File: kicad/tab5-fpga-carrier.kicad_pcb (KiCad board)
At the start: 4 copper layers, 81 x 78 mm, 77 parts, among them J1 DC 12-24V, J2 USB-C PD in, J3 M5-BUS (to Tab5), J4 Tang Primer 20K Core, J5 HDMI OUT, J6 PMOD1, J7 PMOD2, J8 FPGA JTAG, Q1 2N7002, Q2 2N7002, SW1 SW, SW2 SW, U1 CH224K, U2 TPS5430DDAR, U3 AMS1117-3.3

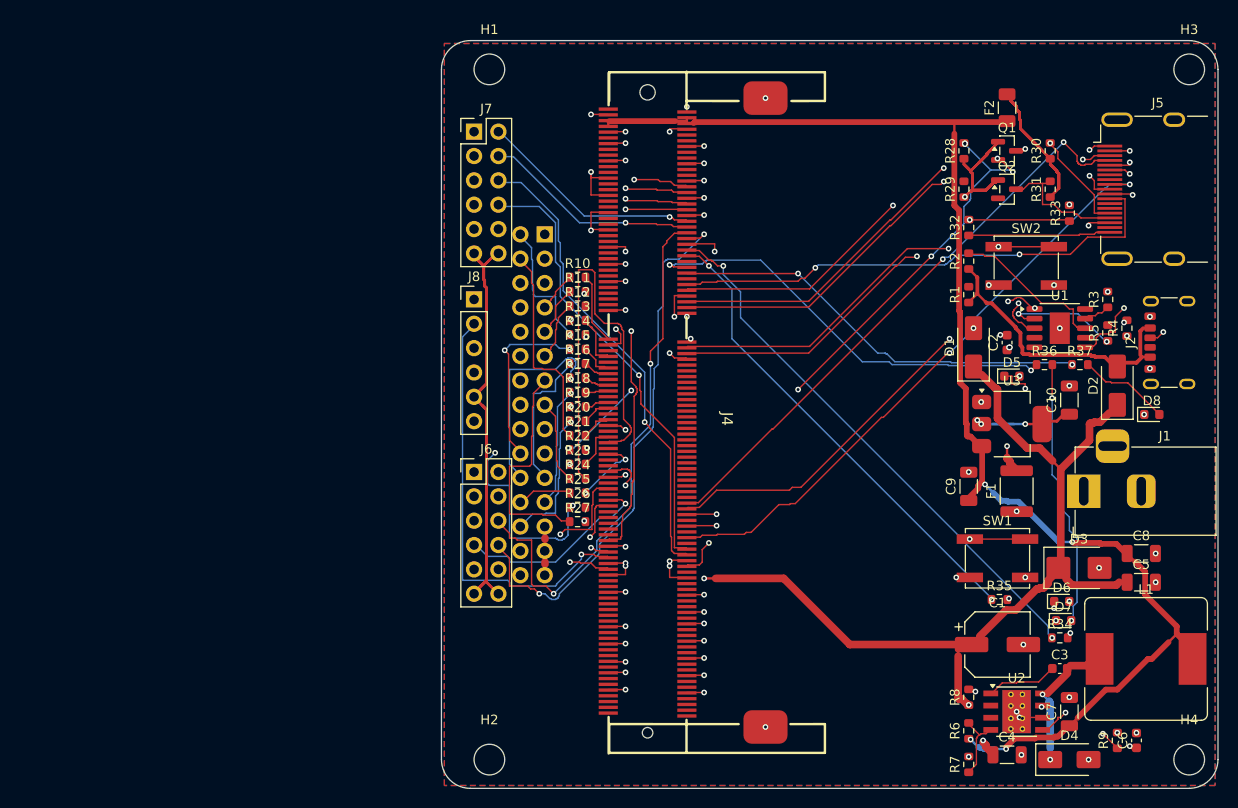
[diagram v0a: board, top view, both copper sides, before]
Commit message: kicad: 103/103 nets routed (rip-up router), DRC clean; BOM; finish script; site update
Co-Authored-By: Claude Sonnet 5.5 <noreply@anthropic.com>
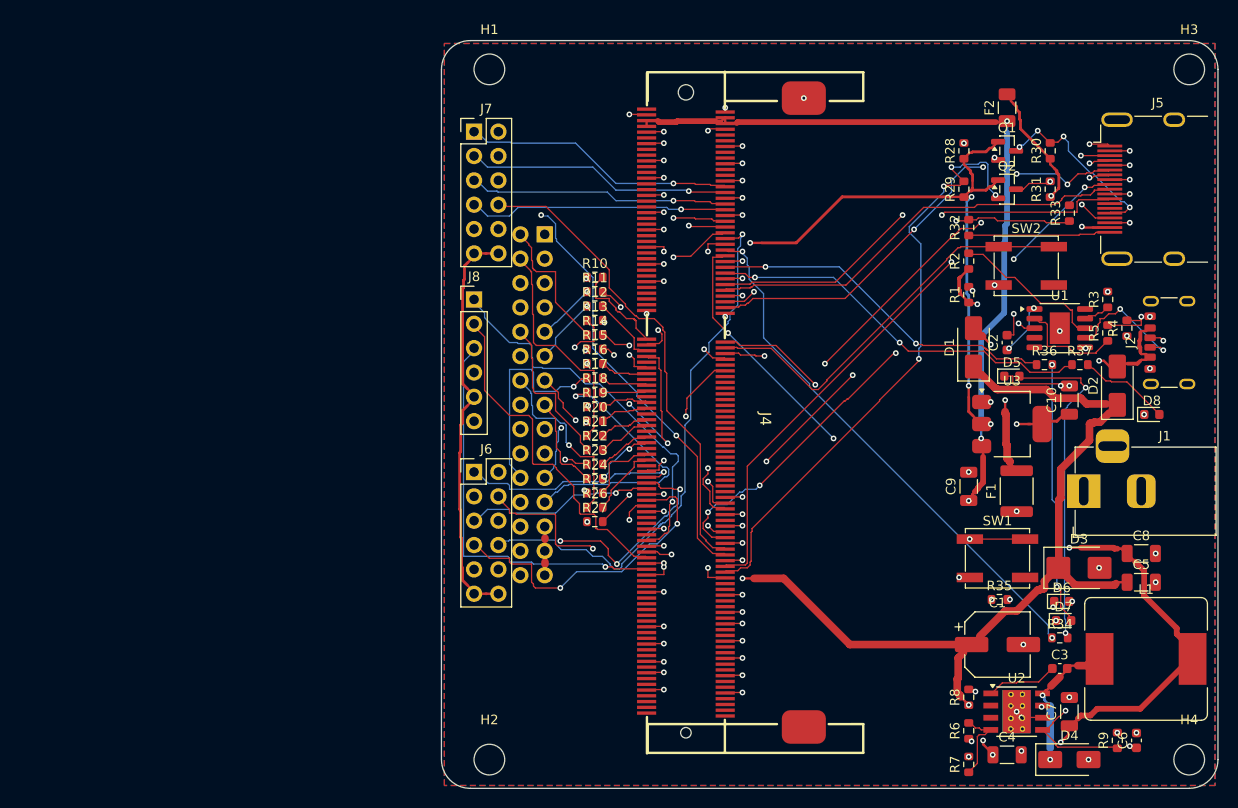
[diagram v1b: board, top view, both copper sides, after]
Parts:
- moved J4 4.00 mm to (71.5, 39.8)
- moved R10 1.80 mm to (62.0, 25.7)
- moved R11 1.80 mm to (62.0, 27.2)
- moved R12 1.80 mm to (62.0, 28.7)
- moved R13 1.80 mm to (62.0, 30.2)
- moved R14 1.80 mm to (62.0, 31.7)
- moved R15 1.80 mm to (62.0, 33.2)
- moved R16 1.80 mm to (62.0, 34.7)
- moved R17 1.80 mm to (62.0, 36.2)
- moved R18 1.80 mm to (62.0, 37.7)
- moved R19 1.80 mm to (62.0, 39.2)
- moved R20 1.80 mm to (62.0, 40.7)
- moved R21 1.80 mm to (62.0, 42.2)
- moved R22 1.80 mm to (62.0, 43.7)
- moved R23 1.80 mm to (62.0, 45.2)
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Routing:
- net +3V3: track 245.8 -> 141.2 mm, vias 4 -> 5
- net F_HSDA: track 0.00 -> 64.1 mm, vias 0 -> 4
- net HDMI_D0P: track 0.00 -> 59.7 mm, vias 0 -> 4
- net P1_5: track 0.00 -> 40.5 mm, vias 0 -> 2
- net F_AUX3: track 45.9 -> 6.64 mm, vias 0 -> 2
- net P1_1: track 0.00 -> 34.4 mm, vias 0 -> 3
- net F_D3: track 5.46 -> 26.3 mm, vias 0 -> 3
- net M_D7: track 12.6 -> 28.9 mm
- net M_AUX1: track 31.5 -> 16.4 mm, vias 2 -> 0
- net CC1: track 0.00 -> 13.5 mm, vias 0 -> 2
- net JT_TDO: track 31.7 -> 44.9 mm
- net GND: track 107.0 -> 120.0 mm, vias 76 -> 82
- net M_DIR: track 14.6 -> 27.0 mm
- net P1_3: track 21.3 -> 33.3 mm, vias 1 -> 2
- net M_EXT37: track 30.2 -> 19.1 mm, vias 2 -> 1
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
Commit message: kicad: layout v1.0 (Core left of M5-Bus, HDMI bottom edge, pin swap), 106/106 routed, DRC clean; reset/power switch/GPIO pads; docs
Co-Authored-By: Claude Sonnet 5.5 <noreply@anthropic.com>
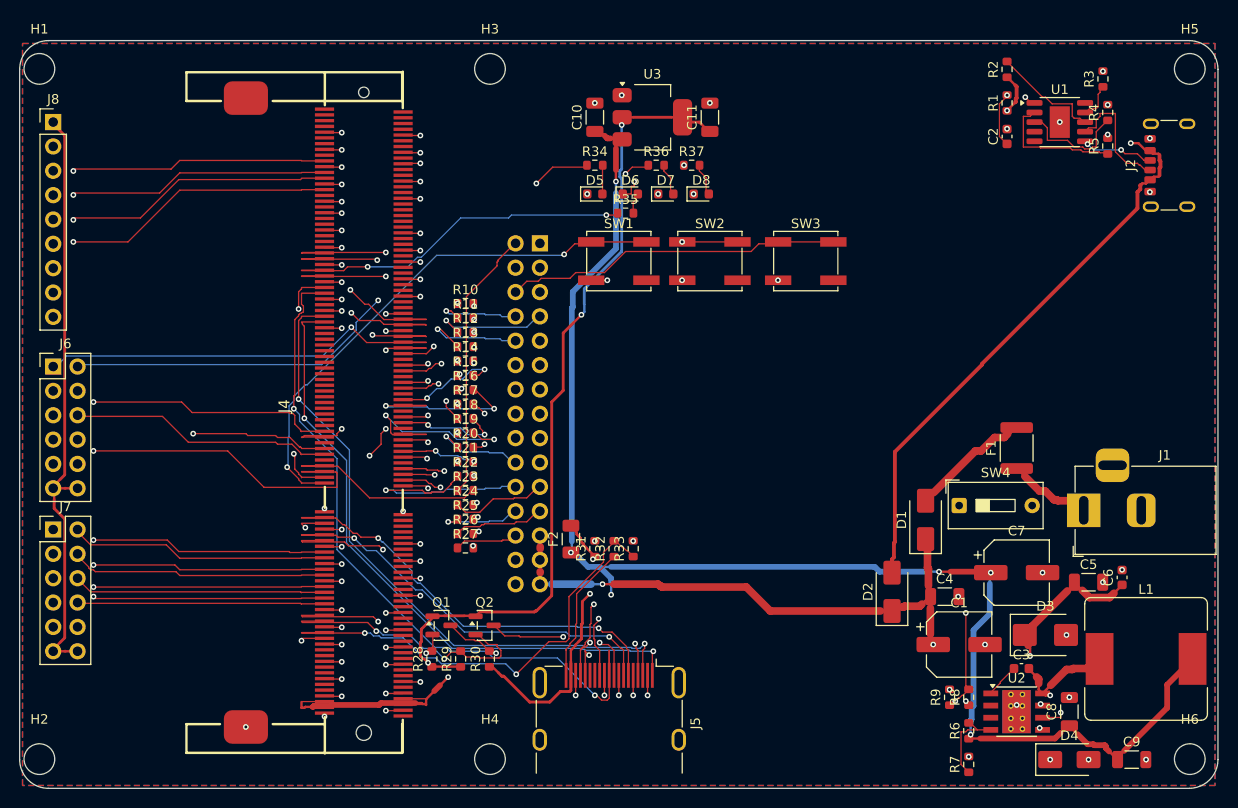
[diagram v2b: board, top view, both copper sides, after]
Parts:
- added C11: 22u/10V, C_1206_3216Metric, F.Cu at (74.0, 9.00)
- added H5: M3, MountingHole_3.2mm_M3, F.Cu at (124.1, 3.95)
- added H6: M3, MountingHole_3.2mm_M3, F.Cu at (124.1, 76.0)
- added SW3: RESET (Tab5), SW_SPST_EVQP0, F.Cu at (84.0, 24.0)
- added SW4: FPGA ON/OFF, SW_DIP_SPSTx01_Slide_9.78x4.72mm_W7.62mm_P2.54mm, F.Cu at (100.0, 49.5)
- C10: value 22u/10V -> 10u/16V
- C7: value 47u/10V -> 220u/10V polymer; footprint C_1206_3216Metric -> CP_Elec_6.3x7.7
- C9: value 10u/16V -> 47u/10V
- J8: value FPGA JTAG -> GPIO pads; footprint PinHeader_1x06_P2.54mm_Vertical -> PinHeader_1x09_P2.54mm_Vertical
- R16, R17: value 33R -> 0R
- R26, R27: value 0R -> 33R
- moved R30 78.9 mm to (51.0, 65.5)
- moved J5 77.4 mm to (63.5, 70.5), turned to -90 degrees
- moved Q1 77.0 mm to (46.0, 62.0)
- moved R28 76.7 mm to (45.0, 65.5)
- moved H3 72.9 mm to (51.1, 3.95)
- moved H4 72.9 mm to (51.1, 76.0)
- moved R29 71.8 mm to (48.0, 65.5)
- moved Q2 71.0 mm to (50.5, 62.0)
- moved R34 69.2 mm to (62.0, 14.0)
- moved F2 64.0 mm to (59.5, 53.0)
- moved D6 61.9 mm to (65.7, 17.0)
- moved D7 60.8 mm to (69.4, 17.0)
- moved R31 60.5 mm to (62.0, 54.0)
- moved J7 60.4 mm to (5.50, 52.0)
- moved C10 57.6 mm to (62.0, 9.00)
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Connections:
- C10 pad 1: +3V3 -> +5V
- J4 pad 101: F_AUX0 -> F_EXT37
- J4 pad 103: F_AUX1 -> F_D2
- J4 pad 107: F_AUX2 -> F_D1
- J4 pad 109: F_AUX3 -> F_AUX1
- J4 pad 113: F_EXT35 -> F_D0
- J4 pad 115: F_EXT37 -> F_RDY
- J4 pad 119: F_EXT38 -> F_AUX0
- J4 pad 121: P1_0 -> P1_4
- J4 pad 123: P1_1 -> P1_0
- J4 pad 125: P1_2 -> GPIO6
- J4 pad 129: P1_3 -> GPIO5
- J4 pad 130: HDMI_D1P -> HDMI_D2P
- J4 pad 131: P1_4 -> GPIO4
- J4 pad 132: HDMI_D1N -> HDMI_D2N
- J4 pad 140: HDMI_D0P -> HDMI_CKP
- J4 pad 142: HDMI_D0N -> HDMI_CKN
- J4 pad 143: JT_TMS -> (no net)
- J4 pad 146: P2_7 -> F_LED0
- J4 pad 147: JT_TDO -> (no net)
- J4 pad 148: P2_6 -> F_LED1
- J4 pad 149: JT_TCK -> (no net)
- J4 pad 152: F_HSCL -> F_LED2
- J4 pad 153: JT_TDI -> (no net)
- J4 pad 154: F_HSDA -> F_LED3
- J4 pad 176: (no net) -> GPIO3
- J4 pad 180: (no net) -> GPIO2
- J4 pad 182: (no net) -> GPIO1
- J4 pad 186: (no net) -> GPIO0
- J4 pad 28: P2_0 -> F_BTN1
- J4 pad 30: P2_1 -> F_HPD
- J4 pad 34: P2_2 -> F_HSDA
- J4 pad 36: P2_3 -> F_HSCL
- J4 pad 40: P2_4 -> P2_7
- J4 pad 42: P2_5 -> P2_3
- J4 pad 44: P1_6 -> P2_6
- J4 pad 46: P1_7 -> P2_2
- J4 pad 50: F_LED0 -> P2_5
- J4 pad 52: F_LED1 -> P2_1
- J4 pad 56: F_LED2 -> P2_4
- J4 pad 58: F_LED3 -> P2_0
- J4 pad 62: HDMI_CKN -> HDMI_D0N
- J4 pad 64: HDMI_CKP -> HDMI_D0P
- J4 pad 68: HDMI_D2P -> HDMI_D1P
- J4 pad 70: HDMI_D2N -> HDMI_D1N
- J4 pad 73: F_D0 -> F_DIR
- J4 pad 75: F_D1 -> F_D7
- J4 pad 76: F_BTN1 -> P1_7
- J4 pad 77: F_D2 -> F_EXT35
- J4 pad 78: F_HPD -> P1_3
- J4 pad 79: F_D3 -> F_D5
- J4 pad 83: F_D4 -> F_D6
- J4 pad 84: P1_5 -> P1_6
- J4 pad 85: F_D5 -> F_D3
- J4 pad 86: (no net) -> P1_2
- J4 pad 89: F_D6 -> F_D4
- J4 pad 90: (no net) -> P1_5
- J4 pad 91: F_D7 -> F_AUX3
- J4 pad 92: (no net) -> P1_1
- J4 pad 95: F_RDY -> F_AUX2
- J4 pad 97: F_DIR -> F_EXT38
- J8 pad 1: JT_TMS -> +3V3
- J8 pad 2: JT_TCK -> GND
- J8 pad 3: JT_TDI -> GPIO0
- J8 pad 4: JT_TDO -> GPIO1
- J8 pad 5: +3V3 -> GPIO2
- J8 pad 6: GND -> GPIO3
- R10 pad 1: M_D0 -> M_AUX0
- R10 pad 2: F_D0 -> F_AUX0
- R11 pad 1: M_D1 -> M_RDY
- R11 pad 2: F_D1 -> F_RDY
- R12 pad 1: M_D2 -> M_D0
- R12 pad 2: F_D2 -> F_D0
- R13 pad 1: M_D3 -> M_AUX1
- R13 pad 2: F_D3 -> F_AUX1
- R14 pad 1: M_CLK -> M_D1
- R14 pad 2: F_CLK -> F_D1
- R15 pad 1: M_D4 -> M_D2
- R15 pad 2: F_D4 -> F_D2
- R16 pad 1: M_D5 -> M_EXT37
- R16 pad 2: F_D5 -> F_EXT37
- R17 pad 1: M_D6 -> M_EXT38
- R17 pad 2: F_D6 -> F_EXT38
- R18 pad 1: M_D7 -> M_AUX2
- R18 pad 2: F_D7 -> F_AUX2
- R19 pad 1: M_RDY -> M_AUX3
- R19 pad 2: F_RDY -> F_AUX3
- R20 pad 1: M_DIR -> M_D4
- R20 pad 2: F_DIR -> F_D4
- R21 pad 1: M_AUX0 -> M_D3
- R21 pad 2: F_AUX0 -> F_D3
- R22 pad 1: M_AUX1 -> M_D6
- R22 pad 2: F_AUX1 -> F_D6
- R23 pad 1: M_AUX2 -> M_CLK
- R23 pad 2: F_AUX2 -> F_CLK
- R24 pad 1: M_AUX3 -> M_D5
- R24 pad 2: F_AUX3 -> F_D5
- R26 pad 1: M_EXT37 -> M_D7
- R26 pad 2: F_EXT37 -> F_D7
- R27 pad 1: M_EXT38 -> M_DIR
- R27 pad 2: F_EXT38 -> F_DIR
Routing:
- net +5V: track 143.0 -> 205.3 mm, vias 6 -> 7
- net VIN: track 144.1 -> 96.2 mm, vias 6 -> 5
- net VBUS_PD: track 30.9 -> 78.0 mm
- net JT_TDO: track 44.9 -> 0.00 mm, vias 1 -> 0
- net +3V3: track 141.2 -> 184.9 mm, vias 5 -> 3
- net GPIO4: track 0.00 -> 43.5 mm, vias 0 -> 1
- net GPIO6: track 0.00 -> 43.2 mm, vias 0 -> 1
- net GPIO5: track 0.00 -> 42.7 mm, vias 0 -> 1
- net JT_TDI: track 42.0 -> 0.00 mm, vias 1 -> 0
- net JT_TMS: track 40.7 -> 0.00 mm, vias 1 -> 0
- net F_HSCL: track 59.9 -> 19.7 mm, vias 3 -> 2
- net F_BTN1: track 42.4 -> 80.7 mm, vias 0 -> 4
- net JT_TCK: track 36.4 -> 0.00 mm
- net TAB_RST: track 0.00 -> 35.4 mm
- net F_HSDA: track 64.1 -> 29.5 mm, vias 4 -> 2
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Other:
- board size 81 x 78 mm -> 125 x 78 mm

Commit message: kicad v2.0: Core right of M-Bus, HDMI right edge, official-Dock HDMI circuit (AC coupling/499R/ESD), coupled TMDS pair routing, 121/121 routed, DRC clean; HDMI SI study + docs/site
Co-Authored-By: Claude Sonnet 5.5 <noreply@anthropic.com>
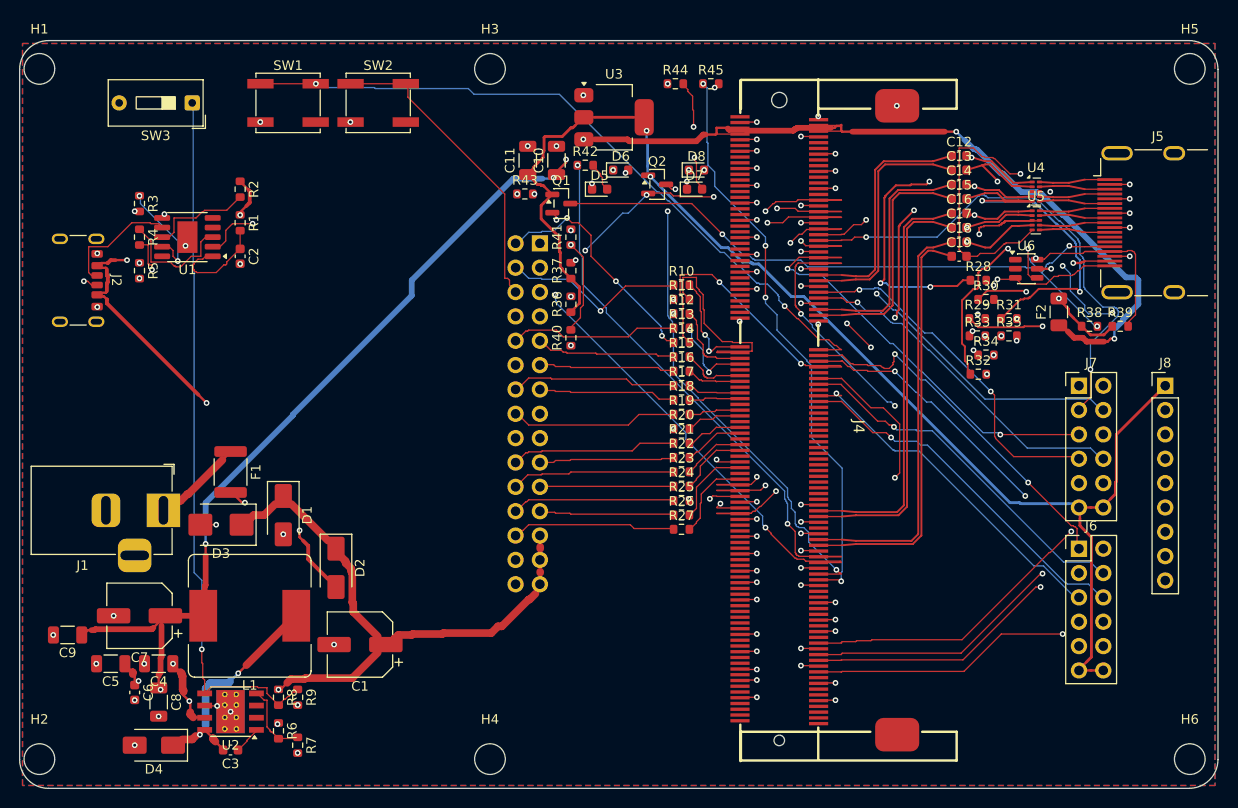
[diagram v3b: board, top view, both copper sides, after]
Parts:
- removed SW4: FPGA ON/OFF, SW_DIP_SPSTx01_Slide_9.78x4.72mm_W7.62mm_P2.54mm
- added C12: 100n, C_0603_1608Metric, F.Cu at (100.0, 13.0)
- added C13: 100n, C_0603_1608Metric, F.Cu at (100.0, 14.5)
- added C14: 100n, C_0603_1608Metric, F.Cu at (100.0, 16.0)
- added C15: 100n, C_0603_1608Metric, F.Cu at (100.0, 17.5)
- added C16: 100n, C_0603_1608Metric, F.Cu at (100.0, 19.0)
- added C17: 100n, C_0603_1608Metric, F.Cu at (100.0, 20.5)
- added C18: 100n, C_0603_1608Metric, F.Cu at (100.0, 22.0)
- added C19: 100n, C_0603_1608Metric, F.Cu at (100.0, 23.5)
- added R38: 2.2k, R_0603_1608Metric, F.Cu at (113.6, 30.8)
- added R39: 2.2k, R_0603_1608Metric, F.Cu at (116.8, 30.8)
- added R40: 10k, R_0603_1608Metric, F.Cu at (59.5, 32.0)
- added R41: 20k, R_0603_1608Metric, F.Cu at (59.5, 21.5)
- added R42: 1k, R_0603_1608Metric, F.Cu at (61.0, 14.0)
- added R43: 1k, R_0603_1608Metric, F.Cu at (54.7, 17.0)
- added R44: 1k, R_0603_1608Metric, F.Cu at (70.4, 5.50)
- added R45: 1k, R_0603_1608Metric, F.Cu at (74.1, 5.50)
- added U4: RCLAMP0524P, USON-10_2.5x1.0mm_P0.5mm, F.Cu at (108.0, 16.8)
- added U5: RCLAMP0524P, USON-10_2.5x1.0mm_P0.5mm, F.Cu at (108.0, 19.8)
- added U6: SRV05-4, SOT-23-6, F.Cu at (107.0, 24.8)
- R16: value 0R -> 33R
- R18: value 33R -> 0R
- R28, R29, R32: value 10k -> 499R
- R30, R31: value 2.2k -> 499R
- R33: value 20k -> 499R
- R34, R35: value 1k -> 499R
- R36, R37: value 1k -> 10k
- SW2: value SW -> RESET (Tab5)
- SW3: value RESET (Tab5) -> FPGA ON/OFF; footprint SW_SPST_EVQP0 -> SW_DIP_SPSTx01_Slide_9.78x4.72mm_W7.62mm_P2.54mm
- moved J8 119.2 mm to (121.5, 37.0)
- moved J2 116.6 mm to (7.00, 26.0), turned to -90 degrees
- moved C9 111.8 mm to (7.00, 63.0), turned to 180 degrees
- moved J6 108.7 mm to (112.5, 54.0)
- moved J7 108.0 mm to (112.5, 37.0)
- moved C6 103.7 mm to (14.0, 69.0), turned to -90 degrees
- moved C5 102.4 mm to (11.5, 66.0), turned to 180 degrees
- moved R4 101.8 mm to (14.5, 21.5), turned to -90 degrees
- moved R5 101.8 mm to (14.5, 25.0), turned to -90 degrees
- moved R3 101.3 mm to (14.5, 18.0), turned to -90 degrees
- moved J1 96.0 mm to (17.0, 50.0), turned to 0 degrees
- moved D4 95.5 mm to (16.0, 74.5), turned to 180 degrees
- moved C8 95.0 mm to (16.5, 70.0), turned to -90 degrees
- moved L1 93.6 mm to (26.0, 61.0), turned to 180 degrees
- moved U1 91.8 mm to (19.5, 21.5), turned to 180 degrees
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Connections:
- J4 pad 101: F_EXT37 -> F_D4
- J4 pad 103: F_D2 -> F_D3
- J4 pad 107: F_D1 -> F_D6
- J4 pad 109: F_AUX1 -> F_D5
- J4 pad 113: F_D0 -> F_EXT35
- J4 pad 115: F_RDY -> F_D7
- J4 pad 119: F_AUX0 -> F_DIR
- J4 pad 121: P1_4 -> P1_3
- J4 pad 123: P1_0 -> P1_7
- J4 pad 125: GPIO6 -> GPIO0
- J4 pad 129: GPIO5 -> GPIO1
- J4 pad 130: HDMI_D2P -> HDMI_D0P
- J4 pad 131: GPIO4 -> GPIO2
- J4 pad 132: HDMI_D2N -> HDMI_D0N
- J4 pad 180: GPIO2 -> GPIO4
- J4 pad 182: GPIO1 -> GPIO5
- J4 pad 186: GPIO0 -> GPIO6
- J4 pad 28: F_BTN1 -> (no net)
- J4 pad 40: P2_7 -> P2_0
- J4 pad 42: P2_3 -> P2_4
- J4 pad 44: P2_6 -> P2_1
- J4 pad 46: P2_2 -> P2_5
- J4 pad 50: P2_5 -> P2_2
- J4 pad 52: P2_1 -> P2_6
- J4 pad 56: P2_4 -> HDMI_D2P
- J4 pad 58: P2_0 -> HDMI_D2N
- J4 pad 62: HDMI_D0N -> P2_3
- J4 pad 64: HDMI_D0P -> P2_7
- J4 pad 73: F_DIR -> F_AUX0
- J4 pad 75: F_D7 -> F_RDY
- J4 pad 76: P1_7 -> P1_0
- J4 pad 77: F_EXT35 -> F_D0
- J4 pad 78: P1_3 -> P1_4
- J4 pad 79: F_D5 -> F_AUX1
- J4 pad 83: F_D6 -> F_D1
- J4 pad 84: P1_6 -> P1_1
- J4 pad 85: F_D3 -> F_D2
- J4 pad 86: P1_2 -> P1_5
- J4 pad 89: F_D4 -> F_EXT37
- J4 pad 90: P1_5 -> P1_2
- J4 pad 91: F_AUX3 -> F_EXT38
- J4 pad 92: P1_1 -> P1_6
- J4 pad 97: F_EXT38 -> F_AUX3
- J5 pad 1: HDMI_D2P -> HDMI_D2P_K
- J5 pad 10: HDMI_CKP -> HDMI_CKP_K
- J5 pad 12: HDMI_CKN -> HDMI_CKN_K
- J5 pad 3: HDMI_D2N -> HDMI_D2N_K
- J5 pad 4: HDMI_D1P -> HDMI_D1P_K
- J5 pad 6: HDMI_D1N -> HDMI_D1N_K
- J5 pad 7: HDMI_D0P -> HDMI_D0P_K
- J5 pad 9: HDMI_D0N -> HDMI_D0N_K
- R14 pad 1: M_D1 -> M_CLK
- R14 pad 2: F_D1 -> F_CLK
- R15 pad 1: M_D2 -> M_D1
- R15 pad 2: F_D2 -> F_D1
- R16 pad 1: M_EXT37 -> M_D2
- R16 pad 2: F_EXT37 -> F_D2
- R17 pad 1: M_EXT38 -> M_EXT37
- R17 pad 2: F_EXT38 -> F_EXT37
- R18 pad 1: M_AUX2 -> M_EXT38
- R18 pad 2: F_AUX2 -> F_EXT38
- R19 pad 1: M_AUX3 -> M_AUX2
- R19 pad 2: F_AUX3 -> F_AUX2
- R20 pad 1: M_D4 -> M_AUX3
- R20 pad 2: F_D4 -> F_AUX3
- R21 pad 1: M_D3 -> M_D4
- R21 pad 2: F_D3 -> F_D4
- R22 pad 1: M_D6 -> M_D3
- R22 pad 2: F_D6 -> F_D3
- R23 pad 1: M_CLK -> M_D6
- R23 pad 2: F_CLK -> F_D6
- R28 pad 1: +3V3 -> HDMI_D2P_C
- R28 pad 2: F_HSCL -> GND
- R29 pad 1: +3V3 -> HDMI_D2N_C
- R29 pad 2: F_HSDA -> GND
- R30 pad 1: HDMI_5V -> HDMI_D1P_C
- R30 pad 2: HDMI_SCL -> GND
- R31 pad 1: HDMI_5V -> HDMI_D1N_C
- R31 pad 2: HDMI_SDA -> GND
- R32 pad 1: HDMI_HPD -> HDMI_D0P_C
- R32 pad 2: F_HPD -> GND
- R33 pad 1: F_HPD -> HDMI_D0N_C
- R34 pad 1: F_LED0 -> HDMI_CKP_C
- R34 pad 2: LED0_A -> GND
- R35 pad 1: F_LED1 -> HDMI_CKN_C
- R35 pad 2: LED1_A -> GND
- R36 pad 1: F_LED2 -> +3V3
- R36 pad 2: LED2_A -> F_HSCL
- R37 pad 1: F_LED3 -> +3V3
- R37 pad 2: LED3_A -> F_HSDA
- SW2 pad 1: F_BTN1 -> TAB_RST
- SW3 pad 1: TAB_RST -> BUCK_EN
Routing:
- net F_BTN1: track 80.7 -> 0.00 mm, vias 4 -> 0
- net HDMI_CKN_C: track 0.00 -> 61.4 mm, vias 0 -> 2
- net HDMI_SCL: track 19.0 -> 74.9 mm, vias 2 -> 4
- net +3V3: track 184.9 -> 138.4 mm, vias 3 -> 2
- net HDMI_HPD: track 14.5 -> 60.1 mm, vias 0 -> 2
- net HDMI_D2N: track 67.1 -> 25.0 mm, vias 2 -> 0
- net HDMI_D2P: track 66.8 -> 25.0 mm, vias 2 -> 0
- net BUCK_EN: track 32.9 -> 73.9 mm, vias 3 -> 1
- net HDMI_D2N_C: track 0.00 -> 40.2 mm, vias 0 -> 2
- net HDMI_D1N_C: track 0.00 -> 39.0 mm, vias 0 -> 2
- net HDMI_D2P_C: track 0.00 -> 37.7 mm, vias 0 -> 4
- net HDMI_CKP_C: track 0.00 -> 37.1 mm, vias 0 -> 4
- net HDMI_SDA: track 27.0 -> 63.3 mm, vias 4 -> 2
- net HDMI_D0N_C: track 0.00 -> 30.5 mm, vias 0 -> 2
- net HDMI_CKP: track 74.1 -> 43.6 mm, vias 2 -> 0
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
